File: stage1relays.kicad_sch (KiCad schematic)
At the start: 17 parts, among them T3 AO3400A, T4 AO3400A, T7 AO3400A

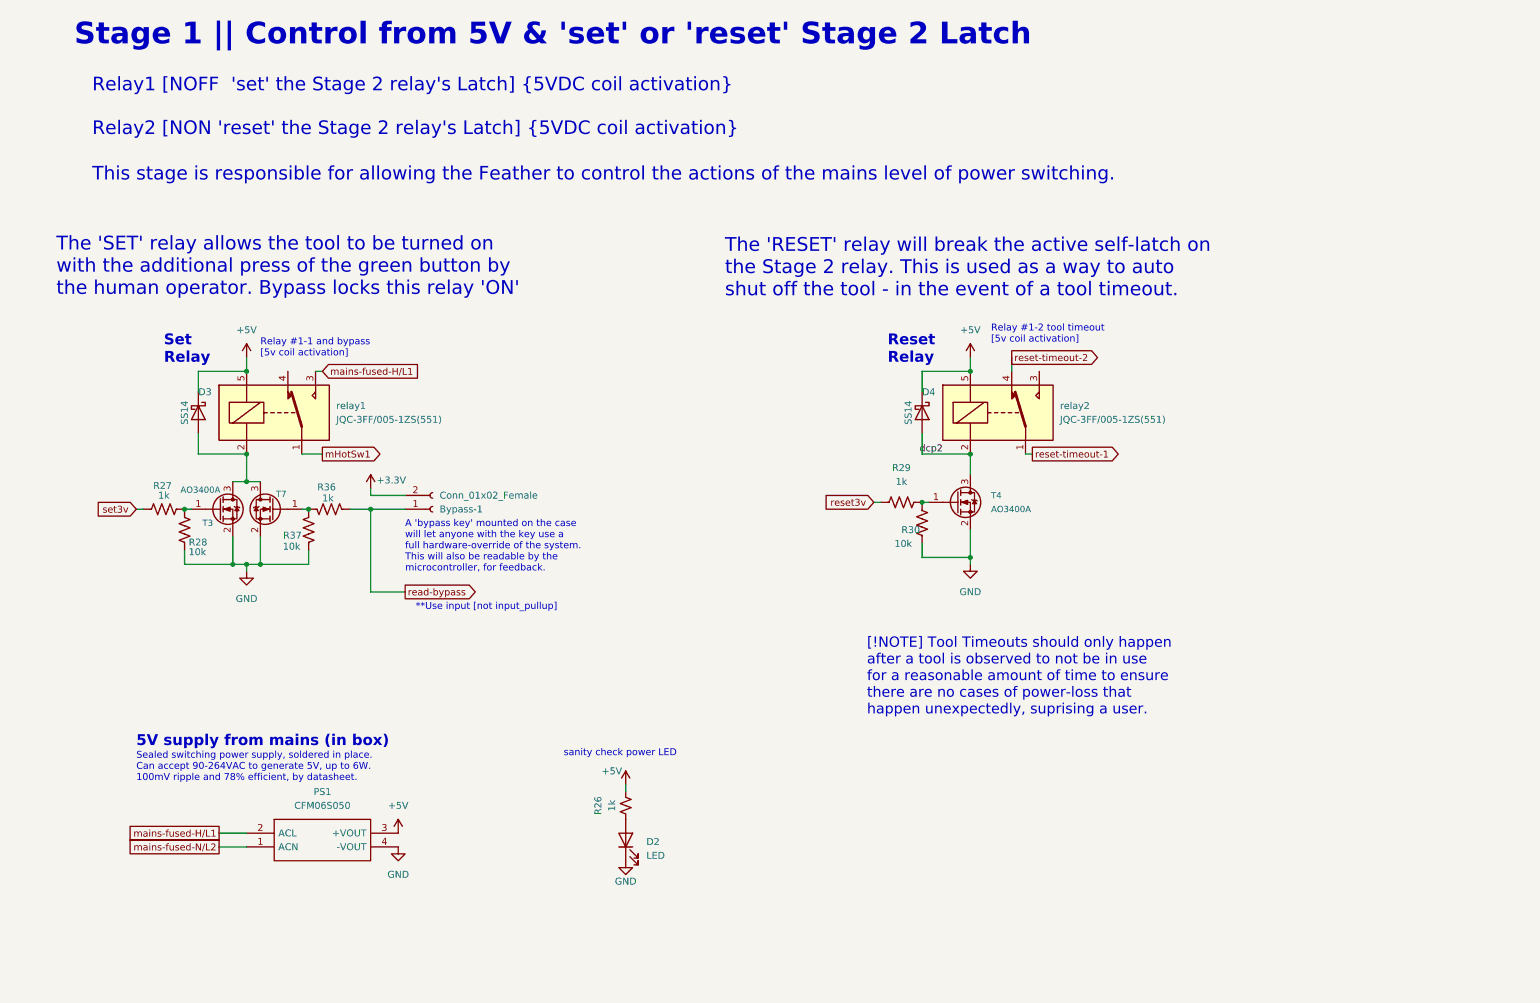
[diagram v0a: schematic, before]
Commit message: bypass key disables reset relay. Based on recommendation from Lior
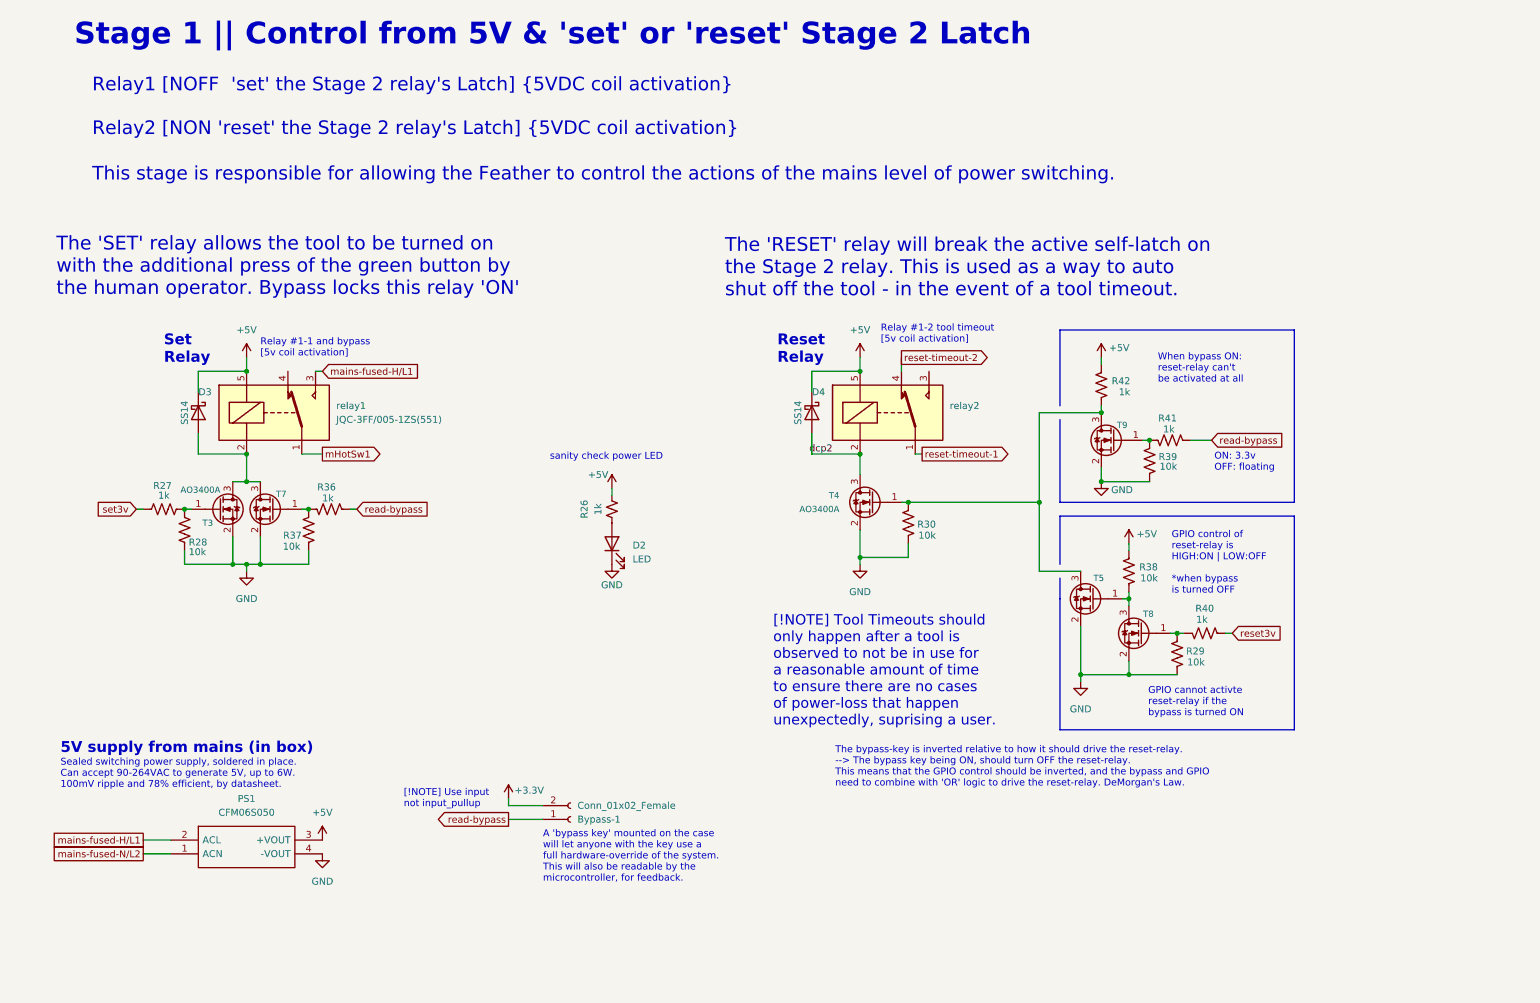
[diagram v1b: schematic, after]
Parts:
- added R38, R39: 10k, Resistor_SMD:R_0603_1608Metric, symbol Device:R_US
- added R40, R41, R42: 1k, Resistor_SMD:R_0603_1608Metric, symbol Device:R_US
- added T5, T8, T9: AO3400A, Package_TO_SOT_SMD:SOT-23, symbol Transistor_FET:AO3400A
- R29: value 1k -> 10k; JLCPCB Part # C21190 -> C25804
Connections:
- net +5V: now also R38.1, R42.1
- net GND: now also R29.2, R39.2, T5.2 (S), T8.2 (S), T9.2 (S)
- net read-bypass: now also R41.1
- net reset3v: now also R40.1; no longer R29.1
- net at R30.1, T4.1 (G): now also R42.2, T5.3 (D), T9.3 (D); no longer R29.2
- new net: R39.1, R41.2, T9.1 (G)
- new net: R29.1, R40.2, T8.1 (G)
- new net: R38.2, T5.1 (G), T8.3 (D)
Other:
- note added: "GPIO cannot activte reset-relay if the bypass is turned ON"
- note added: "GPIO control of reset-relay is HIGH:ON | LOW:OFF *when bypass is turned OFF"
- note added: "ON: 3.3v OFF: floating"
- note added: "The bypass-key is inverted relative to how it should drive the reset-relay. --> The bypass key being ON, should turn OFF the reset-relay. This means that the GPIO control should be inverted, and the bypass and GPIO need to combine with 'OR' logic to drive the reset-relay. DeMorgan's Law."
- note added: "When bypass ON: reset-relay can't be activated at all"
- note added: "[!NOTE] Use input not input_pullup"
- note removed: "**Use input [not input_pullup]"
- moved on the sheet: Bypass-1, D2, D4, PS1, R26, R30, T4, relay2

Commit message: added 74HC02 to stage 1 relay schematic
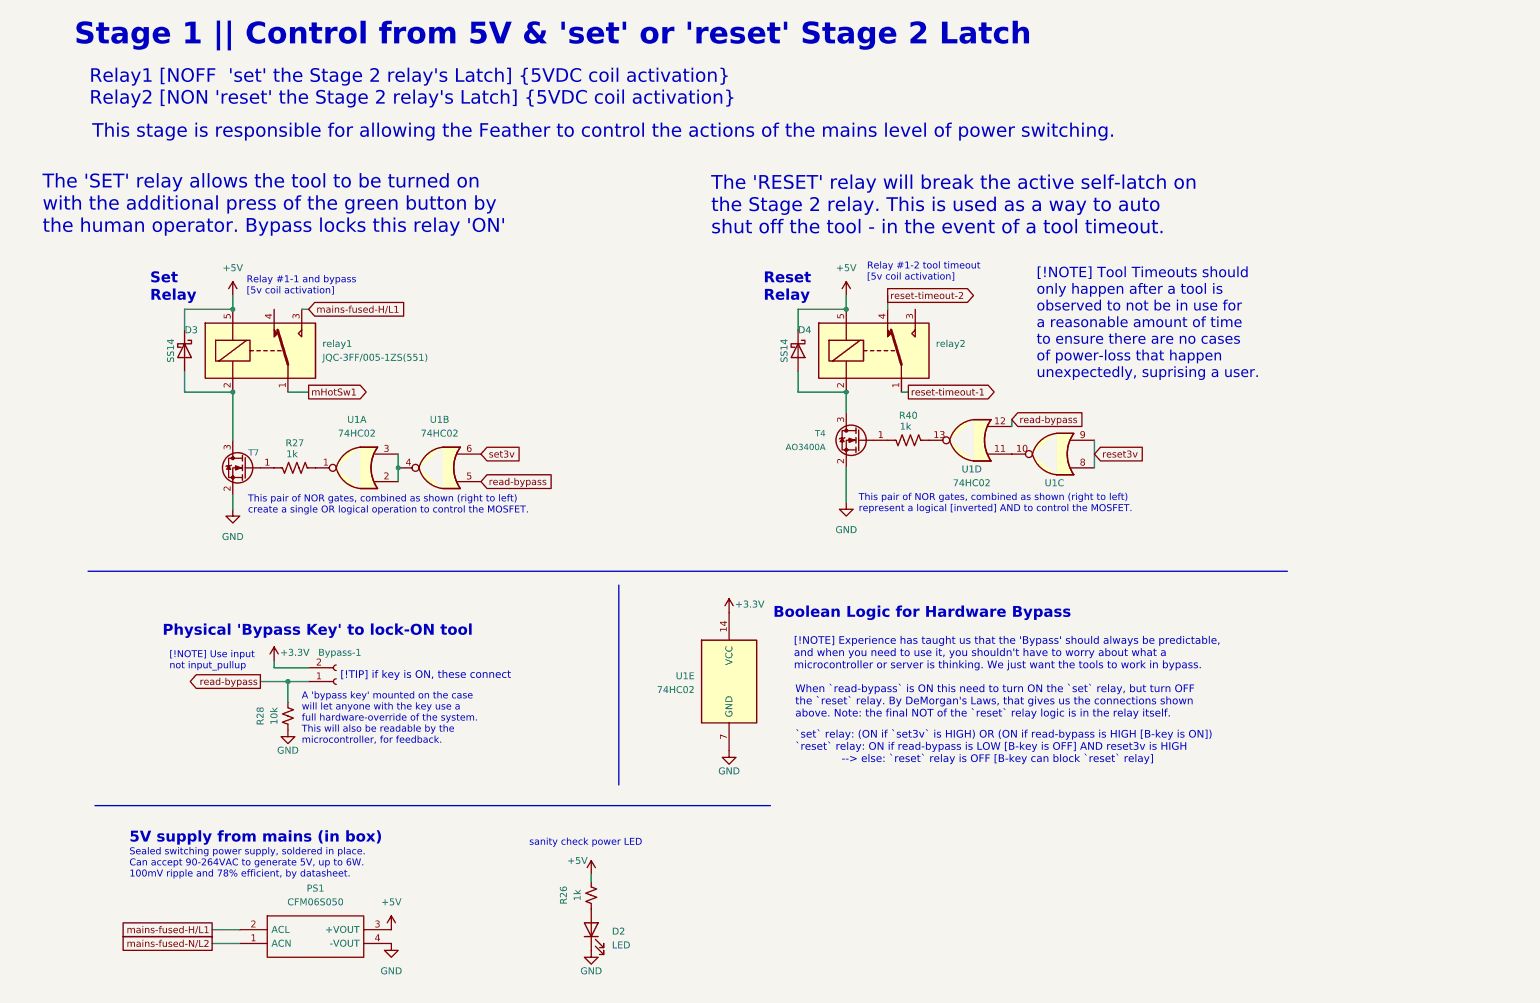
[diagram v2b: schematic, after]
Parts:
- removed R28, R29, R30, R37, R38, R39: 10k, Resistor_SMD:R_0603_1608Metric, symbol Device:R_US
- removed R36, R41, R42: 1k, Resistor_SMD:R_0603_1608Metric, symbol Device:R_US
- removed T3, T5, T8, T9: AO3400A, Package_TO_SOT_SMD:SOT-23, symbol Transistor_FET:AO3400A
- added R28: 10k, Resistor_SMD:R_0603_1608Metric, symbol Device:R_Small_US
- added U1: 74HC02, symbol 74xx:74HC02
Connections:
- net +3.3V: now also U1.14 (VCC)
- net GND: now also R28.1, U1.7 (GND)
- net read-bypass: now also R28.2, U1.12, U1.5
- net reset3v: now also U1.8, U1.9; no longer R40.1
- net set3v: now also U1.6; no longer R27.1
- net at R27.2: now also T7.1 (G)
- net at T4.1 (G): now also R40.2
- net dcp2: no longer names the net of D4.2 (A), T4.3 (D), relay2.2
- new net: R27.1, U1.1
- new net: U1.2, U1.3, U1.4
- new net: U1.10, U1.11
- new net: R40.1, U1.13
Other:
- note added: "Boolean Logic for Hardware Bypass"
- note added: "Physical 'Bypass Key' to lock-ON tool"
- note added: "This pair of NOR gates, combined as shown (right to left) create a single OR logical operation to control the MOSFET."
- note added: "This pair of NOR gates, combined as shown (right to left) represent a logical [inverted] AND to control the MOSFET."
- note added: "When `read-bypass` is ON this need to turn ON the `set` relay, but turn OFF the `reset` relay. By DeMorgan's Laws, that gives us the connections shown above. Note: the final NOT of the `reset` relay logic is in the relay itself."
- note added: "[!NOTE] Experience has taught us that the 'Bypass' should always be predictable, and when you need to use it, you shouldn't have to worry about what a microcontroller or server is thinking. We just want the tools to work in bypass."
- note added: "[!TIP] if key is ON, these connect"
- note added: "`set` relay: (ON if `set3v` is HIGH) OR (ON if read-bypass is HIGH [B-key is ON]) `reset` relay: ON if read-bypass is LOW [B-key is OFF] AND reset3v is HIGH --> else: `reset` relay is OFF [B-key can block `reset` relay]"
- note removed: "GPIO cannot activte reset-relay if the bypass is turned ON"
- note removed: "GPIO control of reset-relay is HIGH:ON | LOW:OFF *when bypass is turned OFF"
- note removed: "ON: 3.3v OFF: floating"
- note removed: "The bypass-key is inverted relative to how it should drive the reset-relay. --> The bypass key being ON, should turn OFF the reset-relay. This means that the GPIO control should be inverted, and the bypass and GPIO need to combine with 'OR' logic to drive the reset-relay. DeMorgan's Law."
- note removed: "When bypass ON: reset-relay can't be activated at all"
- moved on the sheet: Bypass-1, D2, D3, D4, PS1, R26, R40, T4, T7, relay1, relay2

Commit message: update text
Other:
- note added: "The 'RESET' relay will break the active self-latch on the Stage 2 relay. Used as a way to auto shut-off the tool, in event of timeout. Bypass locks this relay 'OFF'"
- note removed: "The 'RESET' relay will break the active self-latch on the Stage 2 relay. This is used as a way to auto shut off the tool - in the event of a tool timeout."
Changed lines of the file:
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@@
 		)
 	)
-	(text "The 'RESET' relay will break the active self-latch on\nthe Stage 2 relay. This is used as a way to auto \nshut off the tool - in the event of a tool timeout."
+	(text "The 'RESET' relay will break the active self-latch on\nthe Stage 2 relay. Used as a way to auto shut-off the \ntool, in event of timeout. Bypass locks this relay 'OFF'"
 		(exclude_from_sim no)
 		(at 145.288 64.008 0)

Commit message: cleanup
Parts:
- U1: footprint (none) -> 74hc02d:SOIC-14_L8.7-W3.9-P1.27-LS6.0-BL
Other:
- moved on the sheet: R40
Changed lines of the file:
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@@
+	(wire
+		(pts
+			(xy 177.8 97.79) (xy 177.8 101.6)
+		)
+		(stroke
+			(width 0)
+			(type default)
+		)
+	)
 	(wire
 		(pts
@@
 		(pts
 			(xy 161.29 81.28) (xy 161.29 77.47)
+		)
+		(stroke
+			(width 0)
+			(type default)
+		)
+	)
+	(wire
+		(pts
+			(xy 185.42 97.79) (xy 185.42 101.6)
 		)
 		(stroke
@@
 			)
 		)
-		(property "Footprint" ""
+		(property "Footprint" "74hc02d:SOIC-14_L8.7-W3.9-P1.27-LS6.0-BL"
 			(at 95.25 106.68 0)
 			(effects
@@
 			)
 		)
-		(property "Footprint" ""
+		(property "Footprint" "74hc02d:SOIC-14_L8.7-W3.9-P1.27-LS6.0-BL"
 			(at 148.59 146.05 0)
 			(effects
@@
 			)
 		)
-		(property "Footprint" ""
+		(property "Footprint" "74hc02d:SOIC-14_L8.7-W3.9-P1.27-LS6.0-BL"
 			(at 193.04 101.6 0)
 			(effects
@@
 			)
 		)
-		(property "Footprint" ""
+		(property "Footprint" "74hc02d:SOIC-14_L8.7-W3.9-P1.27-LS6.0-BL"
 			(at 80.01 106.68 0)
 			(effects
@@
 	(symbol
 		(lib_id "Device:R_US")
-		(at 181.61 101.6 270)
+		(at 181.61 97.79 270)
 		(mirror x)
 		(unit 1)
@@
 		(dnp no)
 		(property "Reference" "R40"
-			(at 181.61 97.028 90)
+			(at 181.61 93.218 90)
 			(effects
 				(font
@@
 		)
 		(property "Value" "1k"
-			(at 181.102 99.06 90)
+			(at 181.102 95.25 90)
 			(effects
 				(font
@@
 		)
 		(property "Footprint" "Resistor_SMD:R_0603_1608Metric"
-			(at 181.356 100.584 90)
+			(at 181.356 96.774 90)
 			(effects
 				(font
@@
 		)
 		(property "Datasheet" "~"
-			(at 181.61 101.6 0)
+			(at 181.61 97.79 0)
 			(effects
 				(font
@@
 		)
 		(property "Description" ""
-			(at 181.61 101.6 0)
+			(at 181.61 97.79 0)
 			(effects
 				(font
@@
 		)
 		(property "JLCPCB Part #" "C21190"
-			(at 181.61 101.6 90)
+			(at 181.61 97.79 90)
 			(effects
 				(font
@@
 			)
 		)
-		(property "Footprint" ""
+		(property "Footprint" "74hc02d:SOIC-14_L8.7-W3.9-P1.27-LS6.0-BL"
 			(at 208.28 104.14 0)
 			(effects
